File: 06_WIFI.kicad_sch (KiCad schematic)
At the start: 0 parts

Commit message: updated schematics
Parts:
- added C601, C602, C606, C611: 4.7uF, Capacitor_SMD:C_0603_1608Metric, symbol Device:C
- added C603: 220nF, Capacitor_SMD:C_0201_0603Metric, symbol Device:C
- added C604, C614: 470nF, Capacitor_SMD:C_0201_0603Metric, symbol Device:C
- added C605, C610, C616, C619: 1.0uF, Capacitor_SMD:C_0402_1005Metric, symbol Device:C
- added C607, C618: 2.2uF, Capacitor_SMD:C_0603_1608Metric, symbol Device:C
- added C608: 10nF, Capacitor_SMD:C_0201_0603Metric, symbol Device:C
- added C609: 2.2uF, Capacitor_SMD:C_0402_1005Metric, symbol Device:C
- added C612, C617: 100nF, Capacitor_SMD:C_0201_0603Metric, symbol Device:C
- added C613: 22nF, Capacitor_SMD:C_0201_0603Metric, symbol Device:C
- added C615: 2.2uF, Capacitor_SMD:C_0201_0603Metric, symbol Device:C
- added L601: 3.3uH_1A_DCR<=200mR, symbol sportwatch_custom:INDUCTOR_2PIN
- added R601, R602: 100k, Resistor_SMD:R_0402_1005Metric, symbol Device:R
- added U10: 2.4/5GHz_DIPLEXER_TBD, symbol sportwatch_custom:WIFI_DIPLEXER
- added U11: TPS22918DBVT, Package_TO_SOT_SMD:SOT-23-6, symbol sportwatch_custom:TPS22918DBV
- added U9: NRF7002-QFAA-R7, QFN48_6X6_NOR, symbol 2026-09-16_06-57-34:NRF7002-QFAA-R
- added Y1: 40MHz_CL8pF_ESR100R_1612, symbol sportwatch_custom:XTAL_2PIN
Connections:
- new net: C616.1, U9.19 (AFELDO)
- new net: C613.1, U9.14 (RFVDD)
- new net: L601.1, U9.26 (BUCKOUT)
- new net: C614.1, U9.11 (SXLDO)
- new net: C611.1, U9.12 (PALDO)
- new net: C612.1, U9.10 (PAVDD<0>), U9.8 (PAVDD<1>)
- new net: C615.1, U9.16 (XOLDO)
- new net: U10.1 (2.4G), U9.9 (TXRF<0>)
- new net: U10.3 (5G), U9.7 (TXRF<1>)
- new net: U9.17 (XOP), Y1.1 (X1)
- new net: U9.18 (XON), Y1.2 (X2)
- new net: C610.2, U9.33 (DIGVDD)
- new net: C608.1, U9.29 (BUCKVMID)
- new net GND: C601.2, C602.2, C603.2, C604.1, C605.2, C606.2, C607.1, C608.2, C609.1, C610.1, C611.2, C612.2, C613.2, C614.2, C615.2, C616.2, C617.2, C618.1, C619.2, R601.2, R602.1, U10.2 (GND), U11.2 (GND), U9.27 (BUCKVSS), U9.28 (BUCKVSS), U9.47 (VSS), U9.49 (VSS)
- new net VBAT: C605.1, C606.1, U9.13 (VBAT), U9.20 (AFEVBAT), U9.25 (BUCKVBAT), U9.31 (BUCKVBATS)
- new net VOUT1_1V8: C619.1, U11.1 (VIN)
- new net WIFI_BUCKEN: R601.1, U9.30 (BUCKEN)
- new net WIFI_COEX_GRANT: U9.43 (COEX_GRANT)
- new net WIFI_COEX_REQ: U9.42 (COEX_REQ)
- new net WIFI_COEX_STATUS: U9.41 (COEX_STATUS0)
- new net WIFI_HOST_IRQ: U9.46 (HOST_IRQ)
- new net WIFI_IOVDD_1V8: C618.2, U11.6 (VOUT), U9.48 (IOVDD)
- new net WIFI_IOVDD_EN: R602.2, U11.3 (ON)
- new net WIFI_PWRIOVDD: C609.2, C617.1, U9.1 (OTPVDD), U9.34 (PWRIOVDD)
- new net WIFI_QSPI_CLK: U9.35 (QSPI_CLK)
- new net WIFI_QSPI_CS: U9.36 (QSPI_SS)
- new net WIFI_QSPI_IO0: U9.37 (QSPI_DATA0)
- new net WIFI_QSPI_IO1: U9.38 (QSPI_DATA1)
- new net WIFI_QSPI_IO2: U9.39 (QSPI_DATA2)
- new net WIFI_QSPI_IO3: U9.40 (QSPI_DATA3)
- new net WIFI_RF: U10.6 (COM)
- new net WIFI_VDD_BUCK: C602.1, C603.1, C604.2, L601.2, U9.15 (RFBUCKVDD), U9.32 (PWRBUCKVDD)
- no-connect marks 0 -> 12
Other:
- note added: "06_WIFI — nRF7002-QFAA-R7 DUAL-BAND WI-FI 6 — REV A"
- note added: "C601/C602/C604/C608 ground returns must follow Nordic isolated-metal-plane guidance near the exposed paddle."
- note added: "COEX_STATUS/REQ/GRANT kept for Wi-Fi/BLE coexistence; SW_CTRL0/1 NC with dedicated Wi-Fi antenna."
- note added: "IMPORTANT: nRF7002 main rail = protected-cell VBAT, NOT nPM1300 VSYS (VSYS can rise near 5 V on VBUS; nRF7002 VBAT recommended max 4.5 V)."
- note added: "Nordic QFN reference capacitor values/package classes are reproduced; exact capacitor MPN/derating is checked at BOM/footprint audit."
- note added: "Nordic QFN reference network / QSPI host / 3-wire BLE coexistence / dedicated Wi-Fi antenna baseline"
- note added: "Power sequence: VBAT present -> wait >=6 ms -> BUCKEN=1 -> wait >=1 ms -> IOVDD_EN=1. Power-down: BUCKEN=0 + IOVDD off before main battery rail disappears."
- note added: "QFN exposed pad pin49 + pin47 VSS are grounded. QFN48_6X6_NOR footprint must be audited before PCB layout."
- note added: "QSPI baseline, max interface clock 32 MHz. Final Apollo peripheral/ball allocation is deferred."
- note added: "TPS22918 U11 switches 1.8 V IOVDD. QOD=VOUT; CT open. R602 and R601 hold IOVDD/BUCKEN off during Apollo reset."
- note added: "U10: required 2.4/5 GHz WLAN diplexer; exact MPN/footprint TBD and selected together with 14_RF."
- note added: "Use protected-cell VBAT for nRF7002 main supply. Do NOT substitute VSYS: nPM1300 can connect VSYS to ~5 V VBUS."
- note added: "WIFI_RF goes to 14_RF. Keep TXRF/diplexer/antenna path very short and copy Nordic RF layout closely."
- note added: "Wi-Fi must be disabled below nRF7002 VBAT minimum 2.9 V. Battery target is nominal 3.7 V / ~4.2 V full."
- note added: "Y1: 40 MHz, SMD1612, CL=8 pF, ESR <=100 ohm. Exact crystal MPN/footprint TBD."
- title: (none) -> Rev-A — Wi-Fi

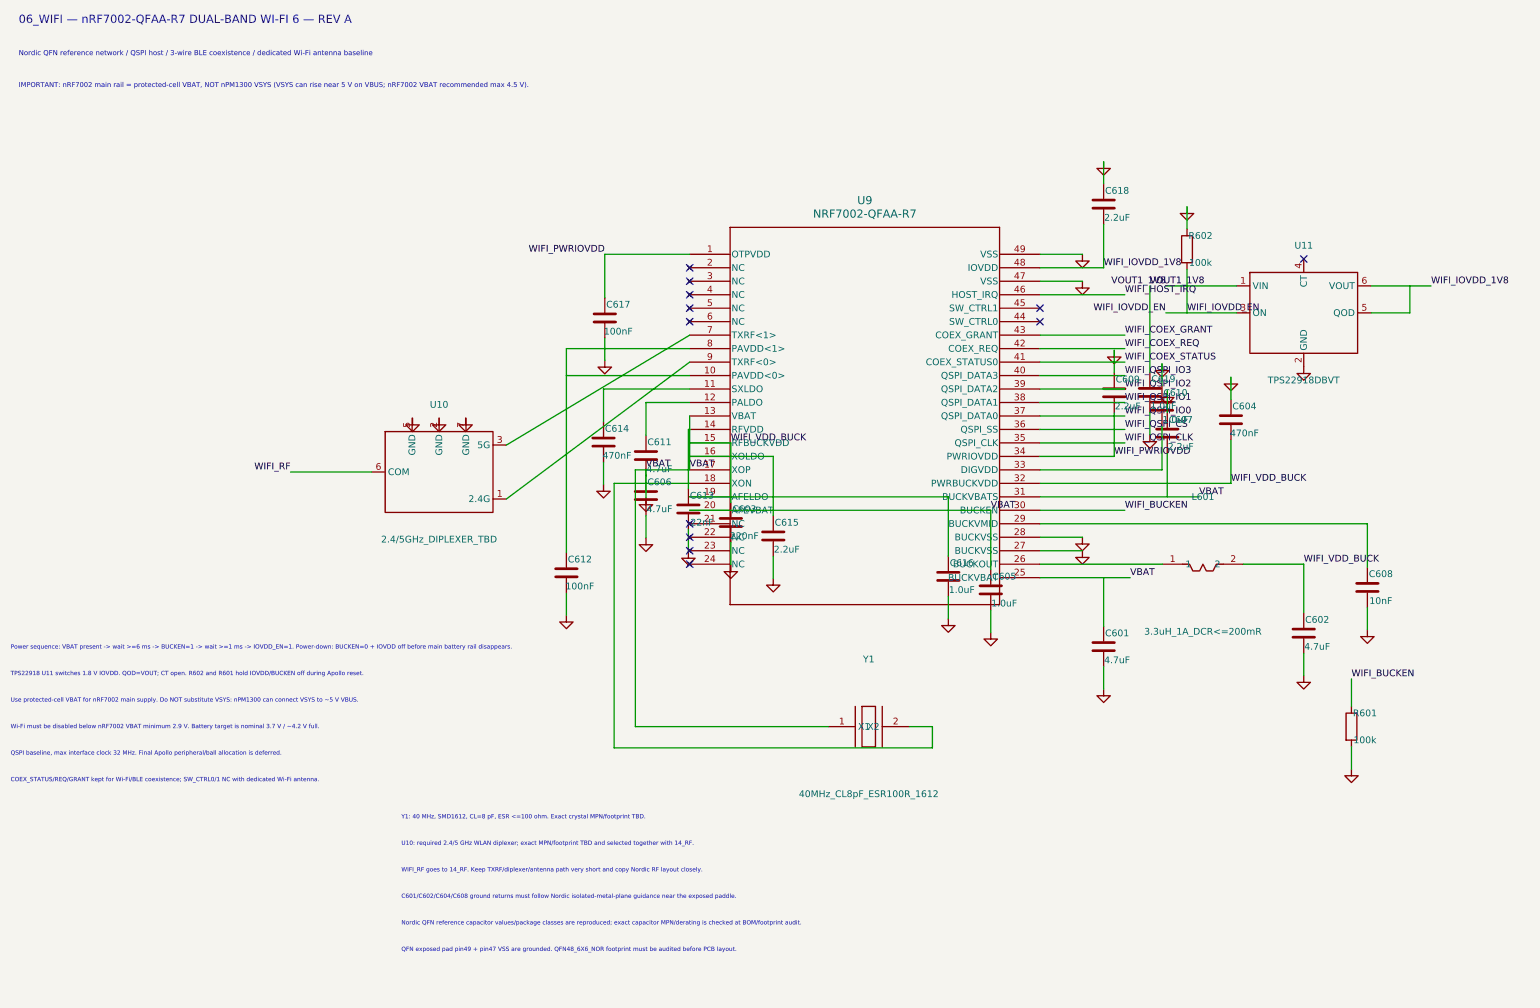
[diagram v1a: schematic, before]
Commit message: refactor(kicad): integrate Rev-A hierarchy and libraries
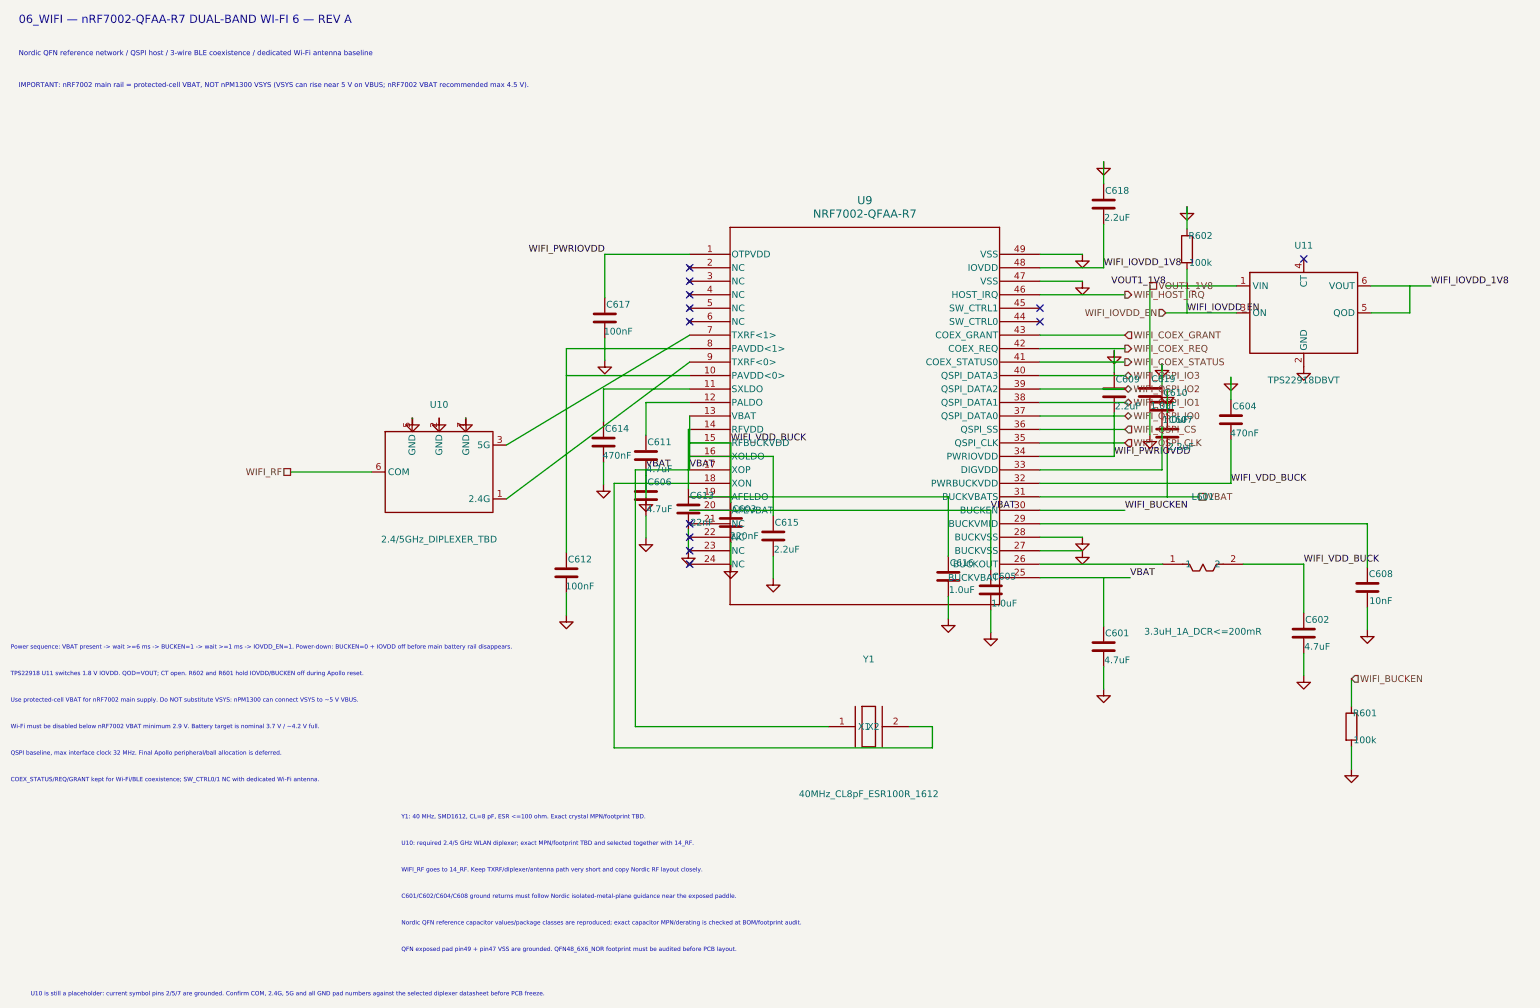
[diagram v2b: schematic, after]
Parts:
- U9: footprint QFN48_6X6_NOR -> sportwatch_custom:QFN48_6X6_NOR
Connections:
- net GND: now also U10.5 (GND), U10.7 (GND)
- net VBAT: now also C601.1, C607.2
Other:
- note added: "U10 is still a placeholder: current symbol pins 2/5/7 are grounded. Confirm COM, 2.4G, 5G and all GND pad numbers against the selected diplexer datasheet before PCB freeze."
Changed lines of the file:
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@@
 	(wire
 		(pts
-			(xy 208.28 121.92) (xy 225.28 121.92)
+			(xy 208.28 121.92) (xy 220.28 121.92)
+		)
+		(stroke
+			(width 0)
+			(type default)
+		)
+	)
+	(wire
+		(pts
+			(xy 220.28 121.92) (xy 225.28 121.92)
 		)
 		(stroke
@@
 	(wire
 		(pts
-			(xy 208.28 106.68) (xy 238.28 106.68)
+			(xy 208.28 106.68) (xy 232.28 106.68)
+		)
+		(stroke
+			(width 0)
+			(type default)
+		)
+	)
+	(wire
+		(pts
+			(xy 232.28 106.68) (xy 238.28 106.68)
 		)
 		(stroke
@@
 		)
 	)
-	(label "WIFI_COEX_STATUS"
+	(hierarchical_label "WIFI_COEX_STATUS"
+		(shape output)
 		(at 224.28 81.28 0)
 		(effects
@@
 		)
 	)
-	(label "WIFI_IOVDD_EN"
+	(hierarchical_label "WIFI_IOVDD_EN"
+		(shape input)
 		(at 232 72 180)
 		(effects
@@
 		)
 	)
-	(label "WIFI_HOST_IRQ"
+	(hierarchical_label "WIFI_HOST_IRQ"
+		(shape output)
 		(at 224.28 68.58 0)
 		(effects
@@
 		)
 	)
-	(label "WIFI_BUCKEN"
+	(hierarchical_label "WIFI_BUCKEN"
+		(shape input)
 		(at 267 141 0)
 		(effects
@@
 		)
 	)
-	(label "VBAT"
+	(hierarchical_label "VBAT"
+		(shape passive)
 		(at 238.28 106.68 0)
 		(effects
@@
 		)
 	)
-	(label "WIFI_QSPI_CLK"
+	(hierarchical_label "WIFI_QSPI_CLK"
+		(shape input)
 		(at 224.28 96.52 0)
 		(effects
@@
 		)
 	)
-	(label "WIFI_QSPI_CS"
+	(hierarchical_label "WIFI_QSPI_CS"
+		(shape input)
 		(at 224.28 93.98 0)
 		(effects
@@
 		)
 	)
-	(label "WIFI_COEX_GRANT"
+	(hierarchical_label "WIFI_COEX_GRANT"
+		(shape input)
 		(at 224.28 76.2 0)
 		(effects
@@
 		)
 	)
-	(label "WIFI_QSPI_IO3"
+	(hierarchical_label "WIFI_QSPI_IO3"
+		(shape bidirectional)
 		(at 224.28 83.82 0)
 		(effects
@@
 		)
 	)
-	(label "VOUT1_1V8"
+	(hierarchical_label "VOUT1_1V8"
+		(shape passive)
 		(at 229 66.92 0)
 		(effects
@@
 		)
 	)
-	(label "WIFI_QSPI_IO2"
+	(hierarchical_label "WIFI_QSPI_IO2"
+		(shape bidirectional)
 		(at 224.28 86.36 0)
 		(effects
@@
 		)
 	)
-	(label "WIFI_RF"
+	(hierarchical_label "WIFI_RF"
+		(shape passive)
 		(at 67 102 180)
 		(effects
@@
 		)
 	)
-	(label "WIFI_QSPI_IO0"
+	(hierarchical_label "WIFI_QSPI_IO0"
+		(shape bidirectional)
 		(at 224.28 91.44 0)
 		(effects
@@
 		)
 	)
-	(label "WIFI_QSPI_IO1"
+	(hierarchical_label "WIFI_QSPI_IO1"
+		(shape bidirectional)
 		(at 224.28 88.9 0)
 		(effects
@@
 		)
 	)
-	(label "WIFI_COEX_REQ"
+	(hierarchical_label "WIFI_COEX_REQ"
+		(shape output)
 		(at 224.28 78.74 0)
 		(effects
@@
 		)
 	)
+	(wire
+		(pts
+			(xy 89.92 91.84) (xy 90 91.84)
+		)
+		(stroke
+			(width 0)
+			(type default)
+		)
+	)
+	(wire
+		(pts
+			(xy 100.08 91.84) (xy 100 91.84)
+		)
+		(stroke
+			(width 0)
+			(type default)
+		)
+	)
 	(symbol
 		(lib_id "Device:C")
@@
 			)
 		)
-		(property "Footprint" "QFN48_6X6_NOR"
+		(property "Footprint" "sportwatch_custom:QFN48_6X6_NOR"
 			(at 142.24 60.96 0)
 			(hide yes)
@@
 		(in_pos_files yes)
 		(dnp no)
-		(property "Reference" "#PWR0610"
+		(property "Reference" "#PWR0622"
 			(at 216.28 114.3 0)
 			(hide yes)
@@
 			(project "sportwatch_revA"
 				(path "/063f9d99-6c07-44cf-ba32-e33897e06972/969e89ce-e77c-4ba6-bffa-a45602245cc9"
-					(reference "#PWR0610")
+					(reference "#PWR0622")
 					(unit 1)
 				)
@@
 		(in_pos_files yes)
 		(dnp no)
-		(property "Reference" "#PWR0603"
+		(property "Reference" "#PWR0623"
 			(at 150 119.52 0)
 			(hide yes)
@@
 			(project "sportwatch_revA"
 				(path "/063f9d99-6c07-44cf-ba32-e33897e06972/969e89ce-e77c-4ba6-bffa-a45602245cc9"
-					(reference "#PWR0603")
+					(reference "#PWR0623")
 					(unit 1)
 				)
@@
 		(in_pos_files yes)
 		(dnp no)
-		(property "Reference" "#PWR0611"
+		(property "Reference" "#PWR0624"
 			(at 134 106.9 0)
 			(hide yes)
@@
 			(project "sportwatch_revA"
 				(path "/063f9d99-6c07-44cf-ba32-e33897e06972/969e89ce-e77c-4ba6-bffa-a45602245cc9"
-					(reference "#PWR0611")
+					(reference "#PWR0624")
 					(unit 1)
 				)
@@
 		(in_pos_files yes)
 		(dnp no)
-		(property "Reference" "#PWR0614"
+		(property "Reference" "#PWR0625"
 			(at 244.28 84.14 0)
 			(hide yes)
@@
 			(project "sportwatch_revA"
 				(path "/063f9d99-6c07-44cf-ba32-e33897e06972/969e89ce-e77c-4ba6-bffa-a45602245cc9"
-					(reference "#PWR0614")
+					(reference "#PWR0625")
 					(unit 1)
 				)
@@
 		)
 	)
+	(text "U10 is still a placeholder: current symbol pins 2/5/7 are grounded. Confirm COM, 2.4G, 5G and all GND pad numbers against the selected diplexer datasheet before PCB freeze."
+		(at 18 201 0)
+		(effects
+			(font
+				(size 0.8 0.8)
+			)
+			(justify left bottom)
+		)
+	)

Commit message: fix(kicad): adjudicate and resolve native ERC errors
- Connect SFH7018A D401.7 and D402.7 green cathode pins to green LED drive
  nets per OSRAM pinout (Class A circuit fix)
- Add deliberate no_connect markers to unused pins U11.5 (QOD) and PMIC U201.15
  (SHPHLD), U201.28 (LSIN1), U201.30 (LSIN2) per datasheets (Class B)
- Place PWR_FLAG markers at external power sources: VBUSIN at J202, VBAT and
  GND at J201 (Class C)
- Place PWR_FLAG markers for net ties and post-inductor domains: PVSS1/PVSS2
  at NT201/NT202, PD_GND at NT401/NT402, and WIFI_VDD_BUCK at L601 (Class D)
- Correct symbol pin electrical types: nRF7002 PAVDD<0>/<1> to passive, PCA9306
  VREF2 to passive, and TC2030-CTX-NL nRESET to passive (Class E)
- Retain U12.A1/U13.A1 PPG_VLED undriven error as intentional TBD (Class G)
- Verification: 83/83 hierarchy interfaces match; ERC errors reduced from 18 to 1
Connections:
- no-connect marks 12 -> 13
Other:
- note added: "TPS22918 U11 switches 1.8 V IOVDD. QOD open; CT open. R602 and R601 hold IOVDD/BUCKEN off during Apollo reset."
- note removed: "TPS22918 U11 switches 1.8 V IOVDD. QOD=VOUT; CT open. R602 and R601 hold IOVDD/BUCKEN off during Apollo reset."
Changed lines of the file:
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@@
 		)
 	)
-	(text "TPS22918 U11 switches 1.8 V IOVDD. QOD=VOUT; CT open. R602 and R601 hold IOVDD/BUCKEN off during Apollo reset."
+	(text "TPS22918 U11 switches 1.8 V IOVDD. QOD open; CT open. R602 and R601 hold IOVDD/BUCKEN off during Apollo reset."
 		(exclude_from_sim no)
 		(at 14.224 140.636 0)
@@
 	)
 	(no_connect
+		(at 270.7 72)
+	)
+	(no_connect
 		(at 142.24 111.76)
 	)
@@
 	(wire
 		(pts
-			(xy 270.7 72) (xy 278 72)
-		)
-		(stroke
-			(width 0)
-			(type default)
-		)
-	)
-	(wire
-		(pts
 			(xy 142.24 101.6) (xy 132 101.6)
 		)
@@
 	(wire
 		(pts
-			(xy 278 72) (xy 278 66.92)
-		)
-		(stroke
-			(width 0)
-			(type default)
-		)
-	)
-	(wire
-		(pts
 			(xy 132 101.6) (xy 132 150)
 		)
@@
 					(unit 1)
 				)
+			)
+		)
+	)
+	(symbol
+		(lib_id "power:PWR_FLAG")
+		(at 258 119.38 0)
+		(unit 1)
+		(body_style 1)
+		(exclude_from_sim no)
+		(in_bom yes)
+		(on_board yes)
+		(in_pos_files yes)
+		(dnp no)
+		(fields_autoplaced yes)
+		(property "Reference" "#FLG0601"
+			(at 258 119.38 0)
+			(hide yes)
+			(show_name no)
+			(do_not_autoplace no)
+			(effects
+				(font
+					(size 1.27 1.27)
+				)
+			)
+		)
+		(property "Value" "PWR_FLAG"
+			(at 258 119.38 0)
+			(show_name no)
+			(do_not_autoplace no)
+			(effects
+				(font
+					(size 1.27 1.27)
+				)
+			)
+		)
+		(property "Footprint" ""
+			(at 258 119.38 0)
+			(hide yes)
+			(show_name no)
+			(do_not_autoplace no)
+			(effects
+				(font
+					(size 1.27 1.27)
+				)
+			)
+		)
+		(property "Datasheet" ""
+			(at 258 119.38 0)
+			(hide yes)
+			(show_name no)
+			(do_not_autoplace no)
+			(effects
+				(font
+					(size 1.27 1.27)
+				)
+			)
+		)
+		(property "Description" ""
+			(at 258 119.38 0)
+			(hide yes)
+			(show_name no)
+			(do_not_autoplace no)
+			(effects
+				(font
+					(size 1.27 1.27)
+				)
+			)
+		)
+		(pin "1"
+		)
+		(instances
+			(project "sportwatch_revA"
+				(path "/063f9d99-6c07-44cf-ba32-e33897e06972/969e89ce-e77c-4ba6-bffa-a45602245cc9"
+					(reference "#FLG0601")
+					(unit 1)
+				)

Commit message: feat(kicad): assign and audit Rev-A footprints
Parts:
- L601: footprint (none) -> sportwatch_custom:L_2016_2016Metric
- Y1: footprint (none) -> sportwatch_custom:Crystal_1612-2Pin_1.6x1.2mm
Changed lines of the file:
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@@
 			)
 		)
-		(property "Footprint" ""
+		(property "Footprint" "sportwatch_custom:L_2016_2016Metric"
 			(at 239 119.38 0)
 			(hide yes)
@@
 			)
 		)
-		(property "Footprint" ""
+		(property "Footprint" "sportwatch_custom:Crystal_1612-2Pin_1.6x1.2mm"
 			(at 176 150 0)
 			(hide yes)

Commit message: fix(pcba): resolve post-footprint freeze sanity items and freeze footprints
- Resolve Flatpak KICAD10_SYMBOL_DIR path discrepancy, reducing lib_symbol_issues to 0
- Re-audit Y1 and Y102 crystals against NDK NX1612SA; ground pads 2/4 for RF shield
- Reclassify SW1..SW5, J201, and J202 as Class C pending mechanical enclosure freeze
- Verify native ERC (0 errors), 83 interfaces (checked=83 mismatches=0), and 0 unintended net changes
- Add docs/project/post_footprint_freeze_sanity.md with FOOTPRINT FREEZE: PASS
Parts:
- Y1: footprint sportwatch_custom:Crystal_1612-2Pin_1.6x1.2mm -> sportwatch_custom:Crystal_1612-4Pin_1.6x1.2mm; symbol sportwatch_custom:XTAL_2PIN -> sportwatch_custom:Crystal_1612-4Pin_GND
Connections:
- net GND: now also Y1.2 (GND), Y1.4 (GND)
- net at U9.18 (XON): now also Y1.3; no longer Y1.2 (X2)
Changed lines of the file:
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@@
 	)
 	(symbol
-		(lib_id "sportwatch_custom:XTAL_2PIN")
+		(lib_id "sportwatch_custom:Crystal_1612-4Pin_GND")
 		(at 176 150 0)
 		(unit 1)
@@
 			)
 		)
-		(property "Footprint" "sportwatch_custom:Crystal_1612-2Pin_1.6x1.2mm"
+		(property "Footprint" "sportwatch_custom:Crystal_1612-4Pin_1.6x1.2mm"
 			(at 176 150 0)
 			(hide yes)
@@
 		(pin "1"
 		)
+		(pin "3"
+		)
 		(pin "2"
+		)
+		(pin "4"
 		)
 		(instances
@@
 					(unit 1)
 				)
+			)
+		)
+	)
+	(symbol
+		(lib_id "power:GND")
+		(at 176 144.92 180)
+		(unit 1)
+		(body_style 1)
+		(exclude_from_sim no)
+		(in_bom yes)
+		(on_board yes)
+		(in_pos_files yes)
+		(dnp no)
+		(property "Reference" "#PWR0691"
+			(at 176 144.92 0)
+			(hide yes)
+			(show_name no)
+			(do_not_autoplace no)
+			(effects
+				(font
+					(size 1.27 1.27)
+				)
+			)
+		)
+		(property "Value" "GND"
+			(at 176 148.73 0)
+			(hide yes)
+			(show_name no)
+			(do_not_autoplace no)
+			(effects
+				(font
+					(size 1.27 1.27)
+				)
+			)
+		)
+		(property "Footprint" ""
+			(at 176 144.92 0)
+			(hide yes)
+			(show_name no)
+			(do_not_autoplace no)
+			(effects
+				(font
+					(size 1.27 1.27)
+				)
+			)
+		)
+		(property "Datasheet" ""
+			(at 176 144.92 0)
+			(hide yes)
+			(show_name no)
+			(do_not_autoplace no)
+			(effects
+				(font
+					(size 1.27 1.27)
+				)
+			)
+		)
+		(property "Description" ""
+			(at 176 144.92 0)
+			(hide yes)
+			(show_name no)
+			(do_not_autoplace no)
+			(effects
+				(font
+					(size 1.27 1.27)
+				)
+			)
+		)
+		(pin "1"
+		)
+		(instances
+			(project "sportwatch_revA"
+				(path "/063f9d99-6c07-44cf-ba32-e33897e06972/969e89ce-e77c-4ba6-bffa-a45602245cc9"
+					(reference "#PWR0691")
+					(unit 1)
+				)
